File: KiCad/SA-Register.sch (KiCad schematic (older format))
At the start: 60 parts, among them U1 74LVC1G04, U10 74LVC1G32, U11 74LVC1G32, U12 74LVC1G32, U13 74LVC1G32, U14 74LVC1G32, U15 74LVC1G32, U16 74LVC1G32, U17 74LVC1G157, U18 74LVC1G157, U19 74LVC1G157, U2 74LVC1G08, U20 74LVC1G157, U21 74LVC1G157, U22 74LVC1G157, U23 74LVC1G157, U24 74LS377, U3 74LVC1G32, U5 74LVC1G32, U6 74LVC1G32, U7 74LVC1G32, U8 74LVC1G32, U9 74LVC1G32

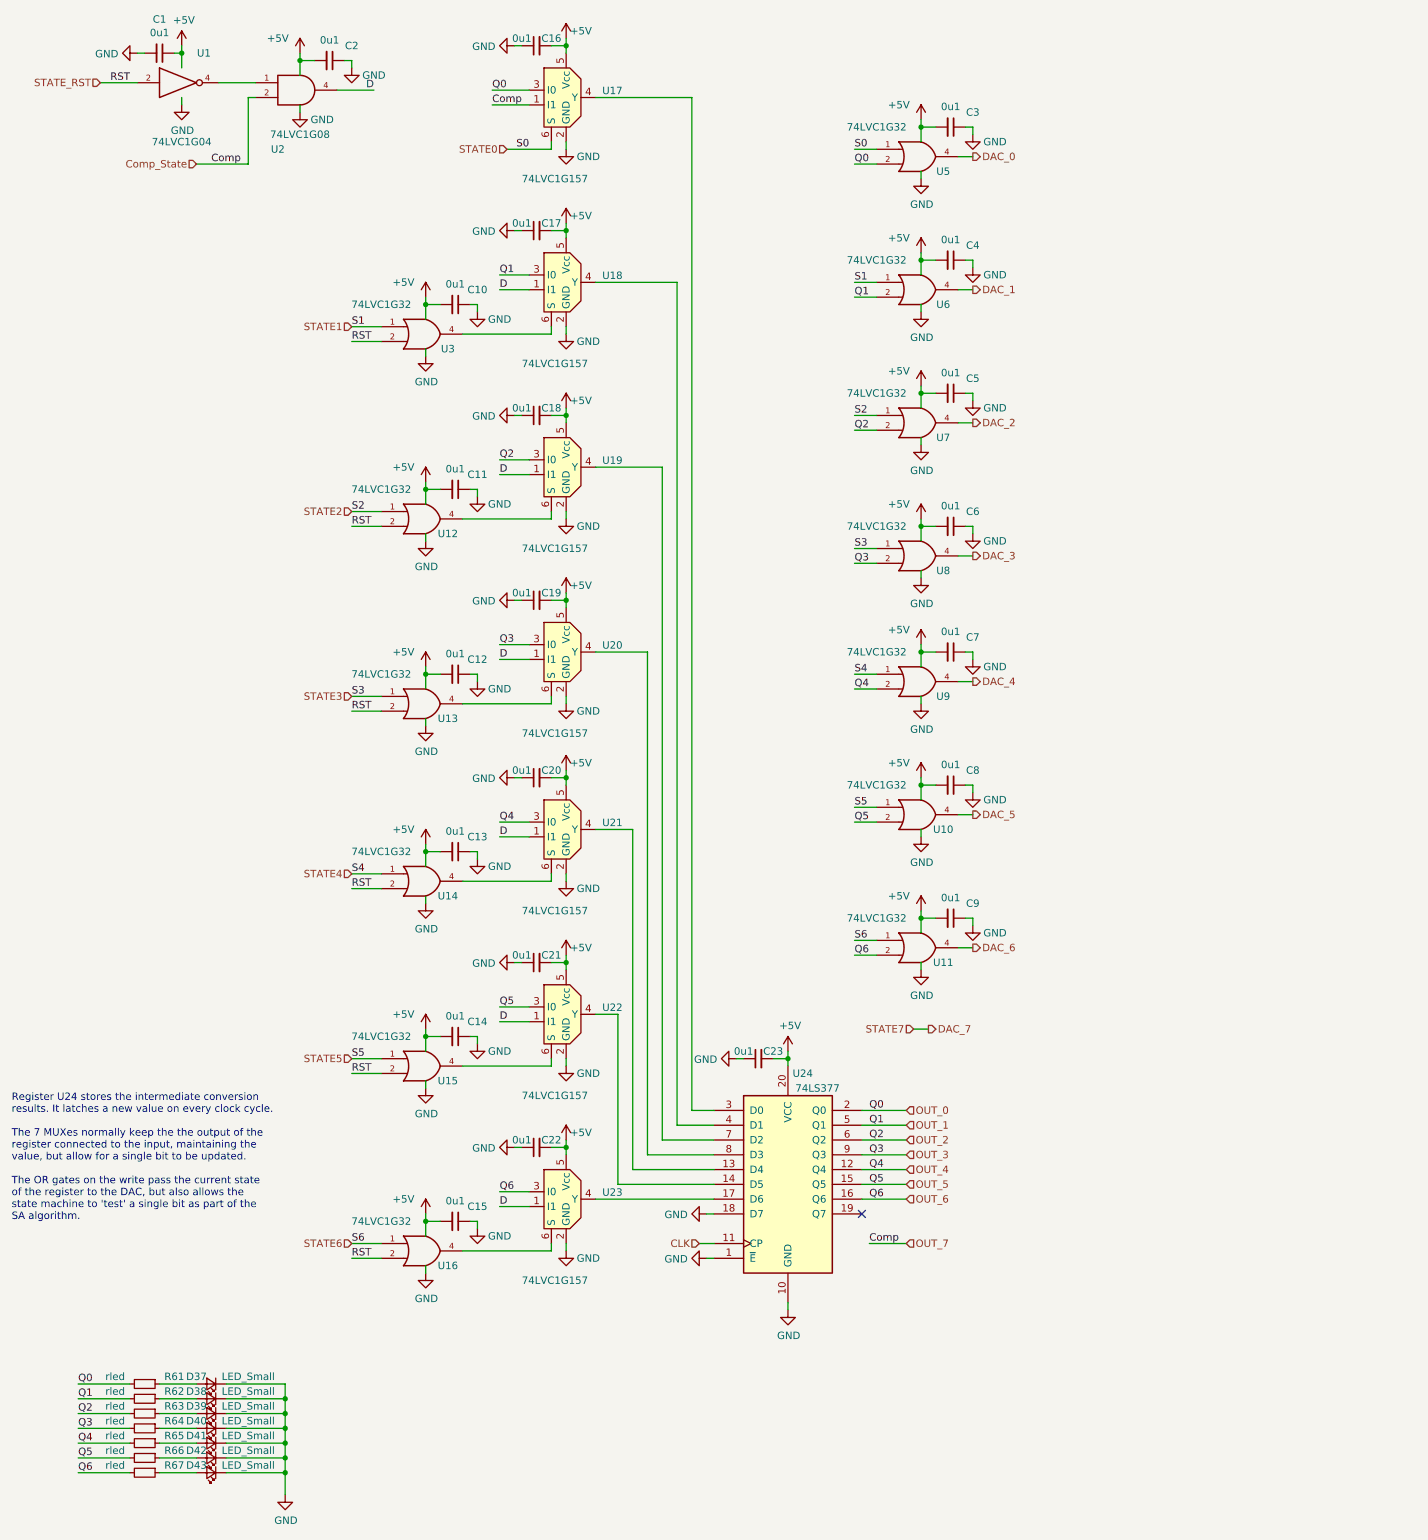
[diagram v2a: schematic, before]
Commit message: Fixed State Numbering/Wiring Order
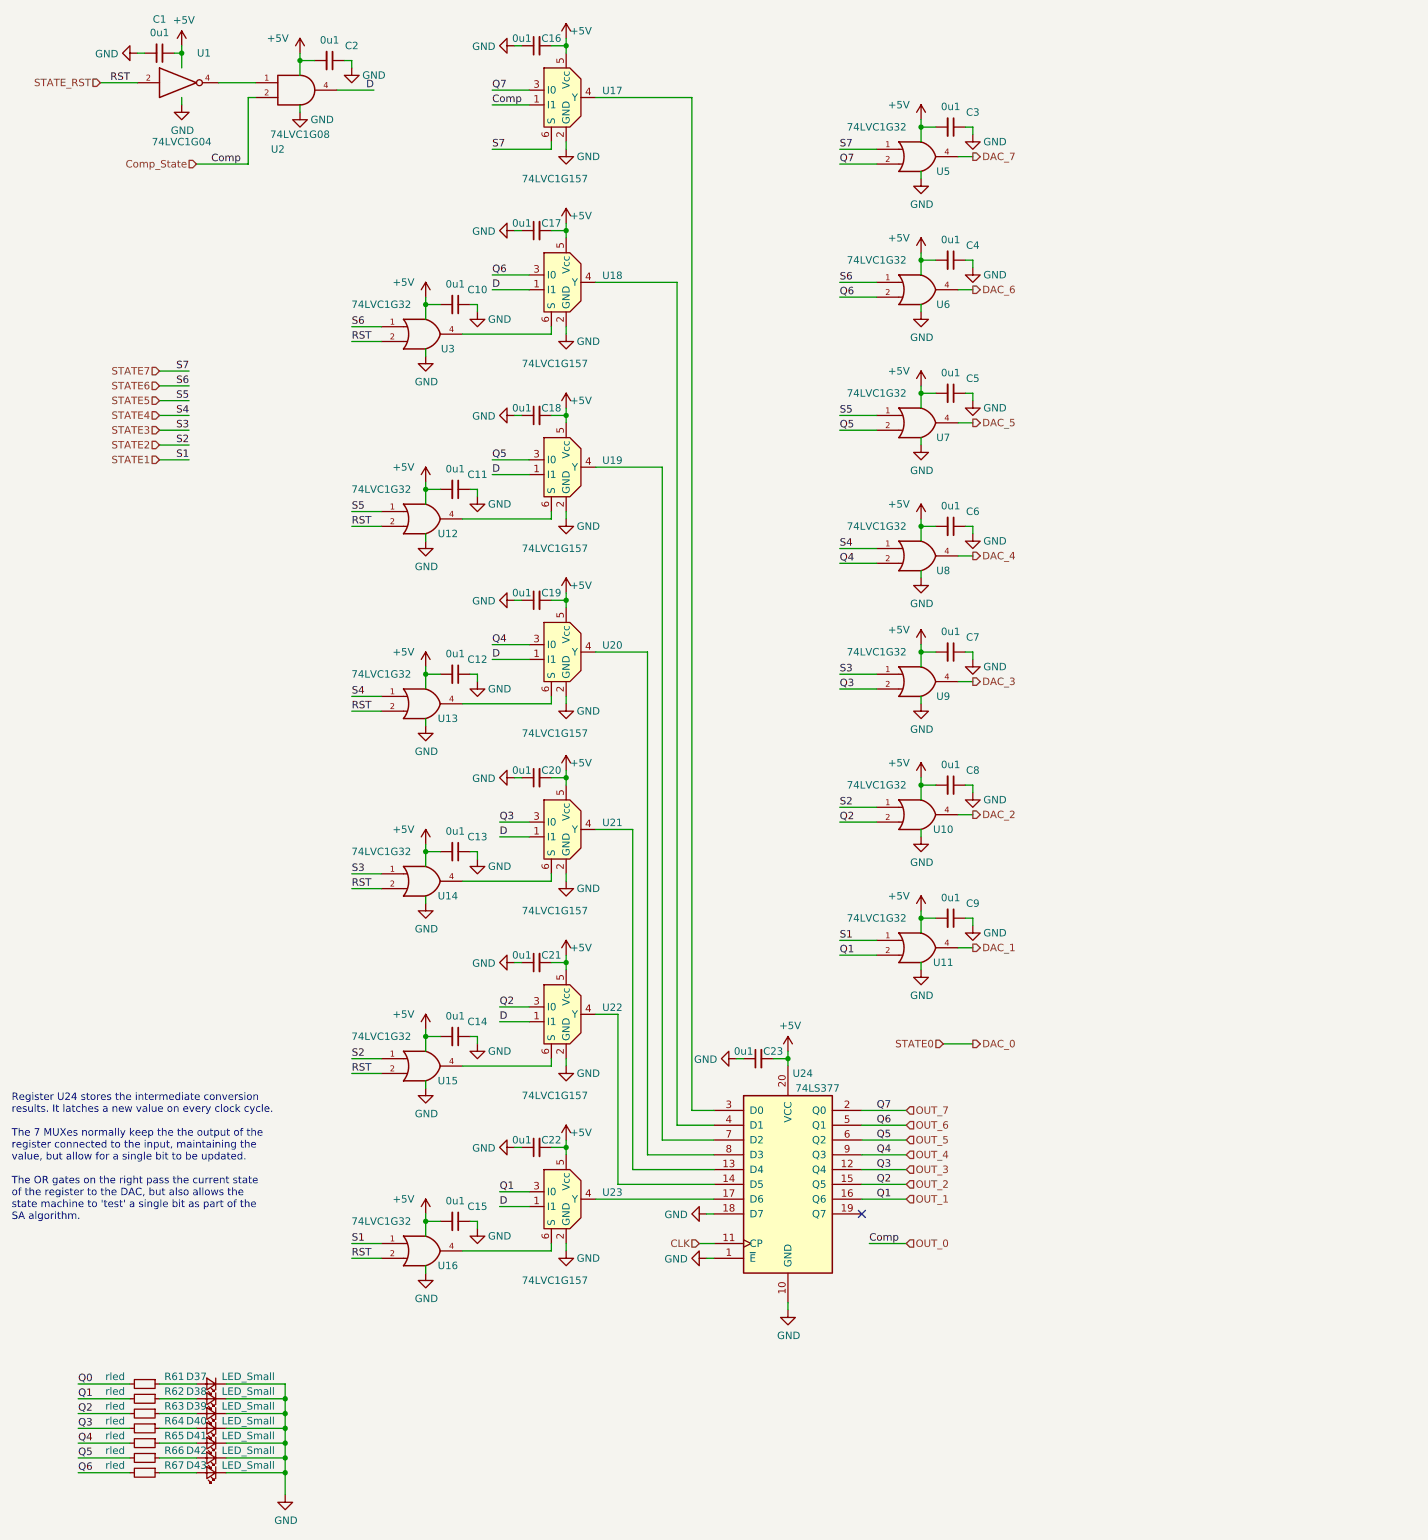
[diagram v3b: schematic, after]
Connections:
- net DAC_0: no longer U5.4
- net DAC_1: now also U11.4; no longer U6.4
- net DAC_2: now also U10.4; no longer U7.4
- net DAC_3: now also U9.4; no longer U8.4
- net DAC_4: now also U8.4; no longer U9.4
- net DAC_5: now also U7.4; no longer U10.4
- net DAC_6: now also U6.4; no longer U11.4
- net DAC_7: now also U5.4
- net OUT_1: now also U11.2, U23.3 (I0), U24.16 (Q6); no longer U18.3 (I0), U24.5 (Q1), U6.2
- net OUT_2: now also U10.2, U22.3 (I0), U24.15 (Q5); no longer U19.3 (I0), U24.6 (Q2), U7.2
- net OUT_3: now also U21.3 (I0), U24.12 (Q4), U9.2; no longer U20.3 (I0), U24.9 (Q3), U8.2
- net OUT_4: now also U20.3 (I0), U24.9 (Q3), U8.2; no longer U21.3 (I0), U24.12 (Q4), U9.2
- net OUT_5: now also U19.3 (I0), U24.6 (Q2), U7.2; no longer U10.2, U22.3 (I0), U24.15 (Q5)
- net OUT_6: now also U18.3 (I0), U24.5 (Q1), U6.2; no longer U11.2, U23.3 (I0), U24.16 (Q6)
- net STATE1: now also U11.1, U16.1; no longer U3.1, U6.1
- net STATE2: now also U10.1, U15.1; no longer U12.1, U7.1
- net STATE3: now also U14.1, U9.1; no longer U13.1, U8.1
- net STATE4: now also U13.1, U8.1; no longer U14.1, U9.1
- net STATE5: now also U12.1, U7.1; no longer U10.1, U15.1
- net STATE6: now also U3.1, U6.1; no longer U11.1, U16.1
- net OUT_0 renamed OUT_7
- net OUT_7: no longer R61.2
- net STATE0 renamed STATE7
- new net Q0: R61.2
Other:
- note added: "Register U24 stores the intermediate conversion\nresults. It latches a new value on every clock cycle.\n\nThe 7 MUXes normally keep the the output of the\nregister connected to the input, maintaining the \nvalue, but allow for a single bit to be updated.\n\nThe OR gates on the right pass the current state\nof the register to the DAC, but also allows the \nstate machine to 'test' a single bit as p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"
- note removed: "Register U24 stores the intermediate conversion\nresults. It latches a new value on every clock cycle.\n\nThe 7 MUXes normally keep the the output of the\nregister connected to the input, maintaining the \nvalue, but allow for a single bit to be updated.\n\nThe OR gates on the write pass the current state\nof the register to the DAC, but also allows the \nstate machine to 'test' a single bit as p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"
